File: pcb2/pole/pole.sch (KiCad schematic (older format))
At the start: 22 parts, among them IC1 LMx93, IC2 STM32F0xxKxUx, P1 POWER_IN, P2 BUS_IN, P3 BUS_OUT, P4 SWD_TC, P5 LEDs, Q1 MTM232270LBF, Q2 MTM232270LBF, Q3 MTM232270LBF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

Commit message: First proof of concept route, with gerbers
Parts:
- added TP1: RST, agg:TESTPAD, symbol TESTPAD
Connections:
- net +3V3: now also C2.1, C3.1, C4.1, C5.1, C8.1, IC2.1 (VDD), IC2.17 (VDD), IC2.5 (VDDA)
- net NRST: no longer IC2.4 (NRST)
- new net: IC2.4 (NRST), TP1.1 (TP)
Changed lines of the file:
@@
 LIBS:swd_tc
 LIBS:stm32f0xxkxux
+LIBS:testpad
 LIBS:pole-cache
 EELAYER 25 0
@@
 	1    0    0    -1
 $EndComp
-Text Label 4500 3000 2    60   ~ 0
-NRST
 Text Label 5500 3600 0    60   ~ 0
 SWDIO
@@
 	1    0    0    -1
 $EndComp
+$Comp
+L +3V3 #PWR029
+U 1 1 56F86196
+P 4200 2500
+F 0 "#PWR029" H 4200 2350 50  0001 C CNN
+F 1 "+3V3" H 4200 2640 50  0000 C CNN
+F 2 "" H 4200 2500 50  0000 C CNN
+F 3 "" H 4200 2500 50  0000 C CNN
+	1    4200 2500
+	1    0    0    -1
+$EndComp
+Connection ~ 4200 2500
+Connection ~ 3850 2400
+$Comp
+L +3V3 #PWR030
+U 1 1 56F861DA
+P 3850 2400
+F 0 "#PWR030" H 3850 2250 50  0001 C CNN
+F 1 "+3V3" H 3850 2540 50  0000 C CNN
+F 2 "" H 3850 2400 50  0000 C CNN
+F 3 "" H 3850 2400 50  0000 C CNN
+	1    3850 2400
+	1    0    0    -1
+$EndComp
+$Comp
+L +3V3 #PWR031
+U 1 1 56F8621A
+P 3400 2300
+F 0 "#PWR031" H 3400 2150 50  0001 C CNN
+F 1 "+3V3" H 3400 2440 50  0000 C CNN
+F 2 "" H 3400 2300 50  0000 C CNN
+F 3 "" H 3400 2300 50  0000 C CNN
+	1    3400 2300
+	1    0    0    -1
+$EndComp
+Connection ~ 3400 2300
+$Comp
+L TESTPAD TP1
+U 1 1 56F866D2
+P 4500 3000
+F 0 "TP1" H 4500 3050 50  0000 L CNN
+F 1 "RST" H 4500 2925 50  0001 L CNN
+F 2 "agg:TESTPAD" H 4500 2850 50  0001 L CNN
+F 3 "" H 4500 3000 50  0001 C CNN
+	1    4500 3000
+	-1   0    0    1
+$EndComp
 $EndSCHEMATC

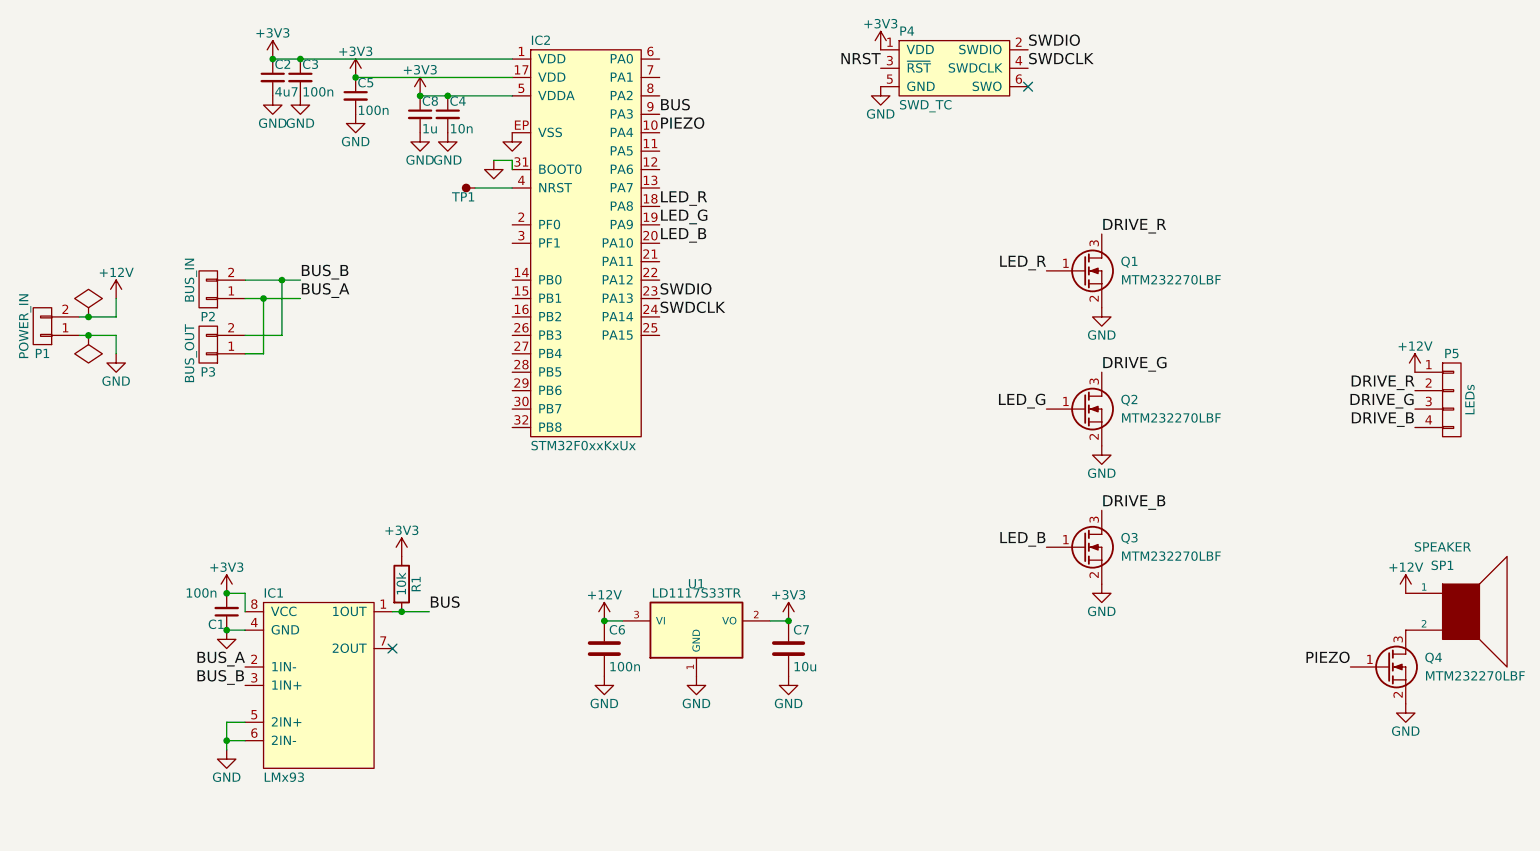
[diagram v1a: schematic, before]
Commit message: Added comparator receiver hysteresis
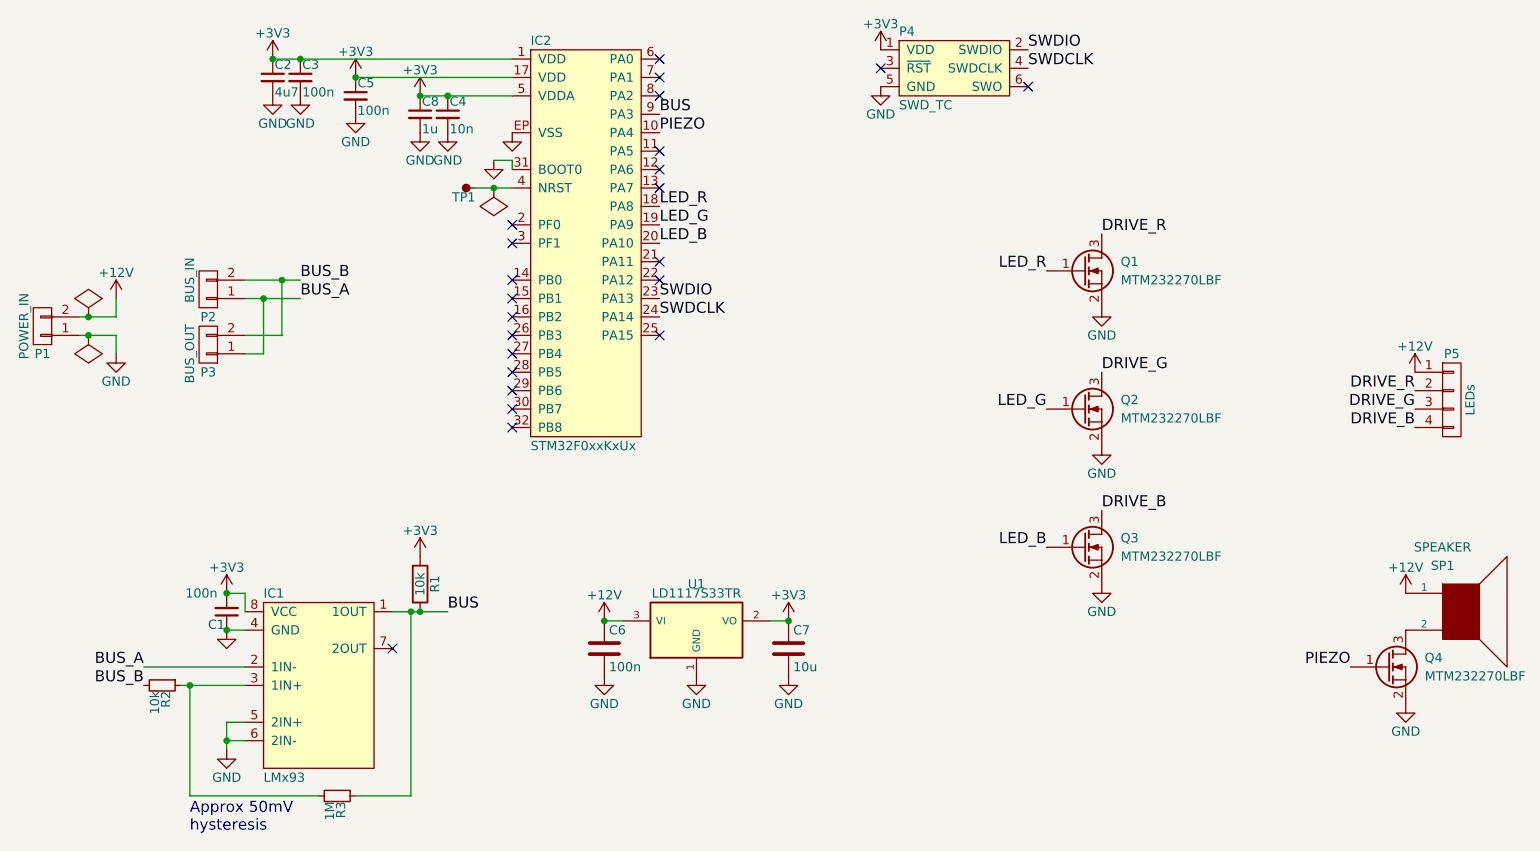
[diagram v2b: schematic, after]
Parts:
- added R2: 10k, agg:0603, symbol R_Small
- added R3: 1M, agg:0603, symbol R_Small
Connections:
- net BUS: now also R3.1
- net BUS_B: now also R2.2; no longer IC1.3 (1IN+)
- net NRST: no longer names the net of P4.3 (~RST)
- new net: IC1.3 (1IN+), R2.1, R3.2
- no-connect marks 2 -> 23
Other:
- note added: "Approx 50mV\nhysteresis"
- moved on the sheet: R1
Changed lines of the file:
@@
 Text Label 3550 3500 0    60   ~ 0
 BUS_B
-Text Label 3250 5600 2    60   ~ 0
+Text Label 2700 5600 2    60   ~ 0
 BUS_A
-Text Label 3250 5700 2    60   ~ 0
+Text Label 2700 5700 2    60   ~ 0
 BUS_B
 $Comp
@@
 	3250 5900 3150 5900
 Connection ~ 3150 6000
-Text Label 4250 5300 0    60   ~ 0
+Text Label 4350 5300 0    60   ~ 0
 BUS
 $Comp
@@
 	1    0    0    -1
 $EndComp
-Text Label 6700 2350 2    60   ~ 0
-NRST
 $Comp
 L C_Small C3
@@
 L R R1
 U 1 1 56F5991E
-P 4100 5150
-F 0 "R1" V 4180 5150 50  0000 C CNN
-F 1 "10k" V 4100 5150 50  0000 C CNN
-F 2 "agg:0603" V 4030 5150 50  0001 C CNN
-F 3 "" H 4100 5150 50  0000 C CNN
-	1    4100 5150
-	1    0    0    -1
-$EndComp
-Wire Wire Line
-	4050 5300 4250 5300
-Connection ~ 4100 5300
+P 4200 5150
+F 0 "R1" V 4280 5150 50  0000 C CNN
+F 1 "10k" V 4200 5150 50  0000 C CNN
+F 2 "agg:0603" V 4130 5150 50  0001 C CNN
+F 3 "" H 4200 5150 50  0000 C CNN
+	1    4200 5150
+	1    0    0    -1
+$EndComp
+Wire Wire Line
+	4050 5300 4350 5300
+Connection ~ 4200 5300
 $Comp
 L +3V3 #PWR016
 U 1 1 56F59A49
-P 4100 5000
-F 0 "#PWR016" H 4100 4850 50  0001 C CNN
-F 1 "+3V3" H 4100 5140 50  0000 C CNN
-F 2 "" H 4100 5000 50  0000 C CNN
-F 3 "" H 4100 5000 50  0000 C CNN
-	1    4100 5000
+P 4200 5000
+F 0 "#PWR016" H 4200 4850 50  0001 C CNN
+F 1 "+3V3" H 4200 5140 50  0000 C CNN
+F 2 "" H 4200 5000 50  0000 C CNN
+F 3 "" H 4200 5000 50  0000 C CNN
+	1    4200 5000
 	1    0    0    -1
 $EndComp
@@
 	-1   0    0    1
 $EndComp
+$Comp
+L R_Small R2
+U 1 1 56F86DEF
+P 2800 5700
+F 0 "R2" H 2830 5720 50  0000 L CNN
+F 1 "10k" H 2830 5660 50  0000 L CNN
+F 2 "agg:0603" H 2800 5700 50  0001 C CNN
+F 3 "" H 2800 5700 50  0000 C CNN
+	1    2800 5700
+	0    1    1    0
+$EndComp
+Wire Wire Line
+	2950 5700 2950 6300
+Wire Wire Line
+	2950 6300 3650 6300
+$Comp
+L R_Small R3
+U 1 1 56F86E8C
+P 3750 6300
+F 0 "R3" H 3780 6320 50  0000 L CNN
+F 1 "1M" H 3780 6260 50  0000 L CNN
+F 2 "agg:0603" H 3750 6300 50  0001 C CNN
+F 3 "" H 3750 6300 50  0000 C CNN
+	1    3750 6300
+	0    1    1    0
+$EndComp
+Wire Wire Line
+	4150 6300 3850 6300
+Wire Wire Line
+	4150 5300 4150 6300
+Connection ~ 4150 5300
+Wire Wire Line
+	2900 5700 3250 5700
+Connection ~ 2950 5700
+Wire Wire Line
+	2700 5600 3250 5600
+NoConn ~ 4700 3500
+NoConn ~ 4700 3600
+NoConn ~ 4700 3700
+NoConn ~ 4700 3800
+NoConn ~ 4700 3900
+NoConn ~ 4700 4000
+NoConn ~ 4700 4100
+NoConn ~ 4700 4200
+NoConn ~ 4700 4300
+NoConn ~ 5500 3800
+NoConn ~ 5500 3500
+NoConn ~ 5500 3400
+NoConn ~ 4700 3200
+NoConn ~ 4700 3300
+NoConn ~ 5500 2800
+NoConn ~ 5500 2900
+NoConn ~ 5500 3000
+NoConn ~ 5500 2300
+NoConn ~ 5500 2400
+NoConn ~ 5500 2500
+NoConn ~ 6700 2350
+$Comp
+L PWR_FLAG #FLG032
+U 1 1 56F88337
+P 4600 3000
+F 0 "#FLG032" H 4600 3095 50  0001 C CNN
+F 1 "PWR_FLAG" H 4600 3180 50  0001 C CNN
+F 2 "" H 4600 3000 50  0000 C CNN
+F 3 "" H 4600 3000 50  0000 C CNN
+	1    4600 3000
+	-1   0    0    1
+$EndComp
+Connection ~ 4600 3000
+Text Notes 2950 6500 0    60   ~ 0
+Approx 50mV\nhysteresis
 $EndSCHEMATC

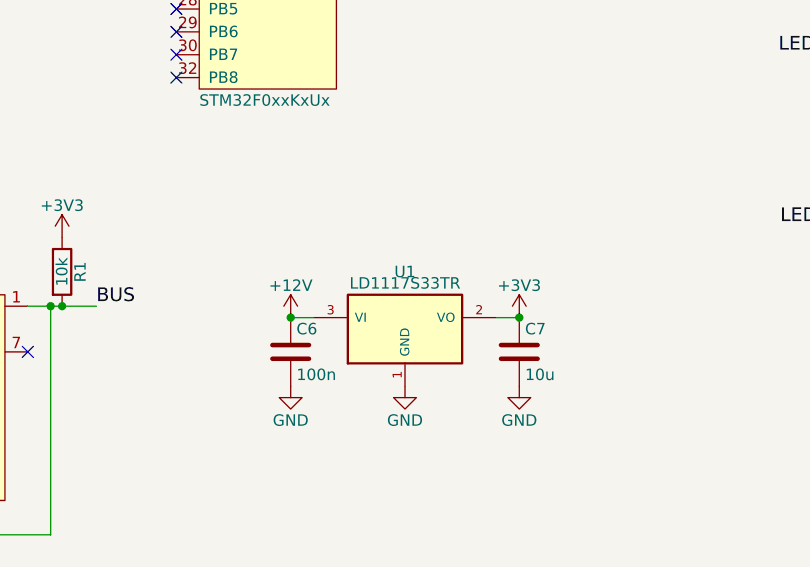
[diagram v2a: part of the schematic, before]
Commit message: Added part numbers and BOMs
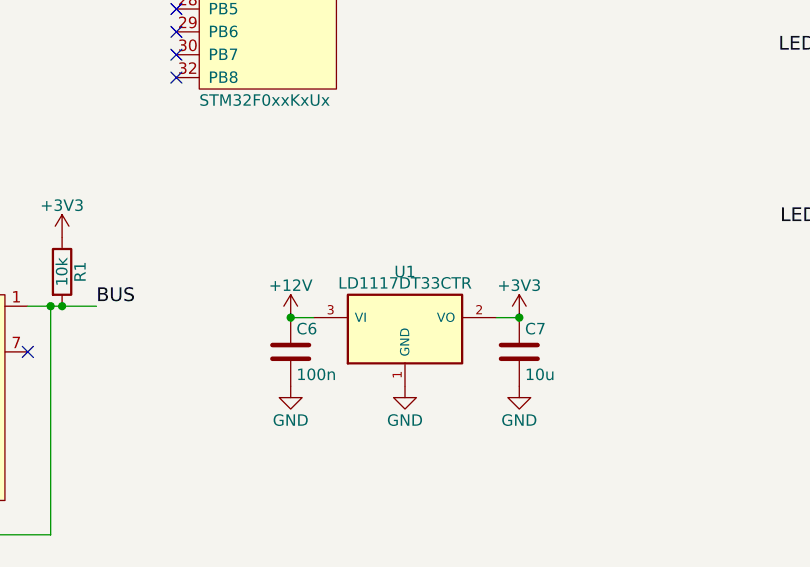
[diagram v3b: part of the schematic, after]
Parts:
- C1, C3, C5, C6: Farnell (none) -> 2496833
- C2: Farnell (none) -> 2496930
- C4: Farnell (none) -> 2496826
- C7: Farnell (none) -> 2494233
- C8: Farnell (none) -> 2496916
- P1: Farnell (none) -> CN18779
- P2, P3: Farnell (none) -> 1830747
- Q1, Q2, Q3, Q4: Farnell (none) -> 2284077
- R1, R2: Farnell (none) -> 9330399
- R3: Farnell (none) -> 9330410
- SP1: Farnell (none) -> 1823866
- U1: value LD1117S33TR -> LD1117DT33CTR; Farnell (none) -> 2296040
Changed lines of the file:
@@
 F 2 "thegrid:minipow_edge" H 2150 3750 50  0001 C CNN
 F 3 "" H 2150 3750 50  0000 C CNN
+F 4 "CN18779" H 2150 3750 60  0001 C CNN "Farnell"
 	1    2150 3750
 	-1   0    0    1
@@
 F 2 "agg:S02B-PASK-2" H 3050 3550 50  0001 C CNN
 F 3 "" H 3050 3550 50  0000 C CNN
+F 4 "1830747" H 3050 3550 60  0001 C CNN "Farnell"
 	1    3050 3550
 	-1   0    0    1
@@
 F 2 "agg:S02B-PASK-2" H 3050 3850 50  0001 C CNN
 F 3 "" H 3050 3850 50  0000 C CNN
+F 4 "1830747" H 3050 3850 60  0001 C CNN "Farnell"
 	1    3050 3850
 	-1   0    0    1
@@
 F 2 "agg:0603" H 3150 5300 50  0001 C CNN
 F 3 "" H 3150 5300 50  0000 C CNN
+F 4 "2496833" H 3150 5300 60  0001 C CNN "Farnell"
 	1    3150 5300
 	-1   0    0    1
@@
 F 2 "agg:0603" H 3550 2400 50  0001 C CNN
 F 3 "" H 3550 2400 50  0000 C CNN
+F 4 "2496833" H 3550 2400 60  0001 C CNN "Farnell"
 	1    3550 2400
 	1    0    0    -1
@@
 F 2 "agg:0603" H 3400 2400 50  0001 C CNN
 F 3 "" H 3400 2400 50  0000 C CNN
+F 4 "2496930" H 3400 2400 60  0001 C CNN "Farnell"
 	1    3400 2400
 	1    0    0    -1
@@
 F 2 "agg:0603" H 4350 2600 50  0001 C CNN
 F 3 "" H 4350 2600 50  0000 C CNN
+F 4 "2496826" H 4350 2600 60  0001 C CNN "Farnell"
 	1    4350 2600
 	1    0    0    -1
@@
 F 1 "SPEAKER" H 9750 5650 50  0000 C CNN
 F 2 "thegrid:piezo" H 9850 5300 50  0001 C CNN
-F 3 "1823866" H 9850 5300 50  0001 C CNN
+F 3 "http://www.farnell.com/datasheets/579045.pdf" H 9850 5300 50  0001 C CNN
+F 4 "1823866" H 9850 5300 60  0001 C CNN "Farnell"
 	1    9850 5300
 	1    0    0    -1
@@
 F 2 "agg:0603" V 4130 5150 50  0001 C CNN
 F 3 "" H 4200 5150 50  0000 C CNN
+F 4 "9330399" H 4200 5150 60  0001 C CNN "Farnell"
 	1    4200 5150
 	1    0    0    -1
@@
 P 5700 5400
 F 0 "U1" H 5700 5650 50  0000 C CNN
-F 1 "LD1117S33TR" H 5700 5600 50  0000 C CNN
+F 1 "LD1117DT33CTR" H 5700 5600 50  0000 C CNN
 F 2 "thegrid:TO-252-3" H 5700 5500 50  0001 C CNN
 F 3 "http://www.farnell.com/datasheets/93498.pdf" H 5700 5400 50  0001 C CNN
+F 4 "2296040" H 5700 5400 60  0001 C CNN "Farnell"
 	1    5700 5400
 	1    0    0    -1
@@
 F 2 "agg:0603" H 5238 5350 50  0001 C CNN
 F 3 "" H 5200 5500 50  0000 C CNN
+F 4 "2496833" H 5200 5500 60  0001 C CNN "Farnell"
 	1    5200 5500
 	1    0    0    -1
@@
 F 2 "agg:0603" H 6238 5350 50  0001 C CNN
 F 3 "" H 6200 5500 50  0000 C CNN
+F 4 "2494233" H 6200 5500 60  0001 C CNN "Farnell"
 	1    6200 5500
 	1    0    0    -1
@@
 F 2 "agg:SOT-323" H 8000 3550 50  0001 C CNN
 F 3 "http://www.farnell.com/datasheets/1916063.pdf" H 7800 3450 50  0001 C CNN
+F 4 "2284077" H 7800 3450 60  0001 C CNN "Farnell"
 	1    7800 3450
 	1    0    0    -1
@@
 F 2 "agg:SOT-323" H 8000 4300 50  0001 C CNN
 F 3 "http://www.farnell.com/datasheets/1916063.pdf" H 7800 4200 50  0001 C CNN
+F 4 "2284077" H 7800 4200 60  0001 C CNN "Farnell"
 	1    7800 4200
 	1    0    0    -1
@@
 F 2 "agg:SOT-323" H 8000 5050 50  0001 C CNN
 F 3 "http://www.farnell.com/datasheets/1916063.pdf" H 7800 4950 50  0001 C CNN
+F 4 "2284077" H 7800 4950 60  0001 C CNN "Farnell"
 	1    7800 4950
 	1    0    0    -1
@@
 F 2 "agg:SOT-323" H 9650 5700 50  0001 C CNN
 F 3 "http://www.farnell.com/datasheets/1916063.pdf" H 9450 5600 50  0001 C CNN
+F 4 "2284077" H 9450 5600 60  0001 C CNN "Farnell"
 	1    9450 5600
 	1    0    0    -1
@@
 F 2 "agg:0603" H 4200 2600 50  0001 C CNN
 F 3 "" H 4200 2600 50  0000 C CNN
+F 4 "2496916" H 4200 2600 60  0001 C CNN "Farnell"
 	1    4200 2600
 	1    0    0    -1
@@
 F 2 "agg:0603" H 3850 2500 50  0001 C CNN
 F 3 "" H 3850 2500 50  0000 C CNN
+F 4 "2496833" H 3850 2500 60  0001 C CNN "Farnell"
 	1    3850 2500
 	1    0    0    -1
@@
 F 2 "agg:0603" H 2800 5700 50  0001 C CNN
 F 3 "" H 2800 5700 50  0000 C CNN
+F 4 "9330399" H 2800 5700 60  0001 C CNN "Farnell"
 	1    2800 5700
 	0    1    1    0
@@
 F 2 "agg:0603" H 3750 6300 50  0001 C CNN
 F 3 "" H 3750 6300 50  0000 C CNN
+F 4 "9330410" H 3750 6300 60  0001 C CNN "Farnell"
 	1    3750 6300
 	0    1    1    0

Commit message: BOM stuff
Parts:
- IC1: footprint SOIC-8 -> agg:SOIC-8
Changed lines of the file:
@@
 F 0 "IC1" H 3350 6200 50  0000 L CNN
 F 1 "LMx93" H 3350 5200 50  0000 L CNN
-F 2 "SOIC-8" H 3350 5100 50  0001 L CNN
+F 2 "agg:SOIC-8" H 3350 5100 50  0001 L CNN
 F 3 "http://www.ti.com/lit/ds/symlink/lm393.pdf" H 3350 5000 50  0001 L CNN
 F 4 "2342314" H 3350 4900 50  0001 L CNN "Farnell"
